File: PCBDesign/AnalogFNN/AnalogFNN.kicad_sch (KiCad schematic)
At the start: 7 parts, among them J1 Conn_01x04_Male, J2 Conn_01x05_Male, SW1 SW_SPDT, U1 STM32F030CCTx

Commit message: Finished neuron placement, laying out weight control modules
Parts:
- added J3: Conn_01x36_Male, Connector_PinHeader_1.00mm:PinHeader_1x36_P1.00mm_Vertical, symbol Connector:Conn_01x36_Male
- added J4: Conn_01x06_Male, Connector_PinHeader_1.00mm:PinHeader_1x06_P1.00mm_Vertical, symbol Connector:Conn_01x06_Male
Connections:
- new net L1_IN1: J3.1 (Pin_1)
- new net L1_IN10: J3.10 (Pin_10)
- new net L1_IN11: J3.11 (Pin_11)
- new net L1_IN12: J3.12 (Pin_12)
- new net L1_IN13: J3.13 (Pin_13)
- new net L1_IN14: J3.14 (Pin_14)
- new net L1_IN15: J3.15 (Pin_15)
- new net L1_IN16: J3.16 (Pin_16)
- new net L1_IN17: J3.17 (Pin_17)
- new net L1_IN18: J3.18 (Pin_18)
- new net L1_IN19: J3.19 (Pin_19)
- new net L1_IN2: J3.2 (Pin_2)
- new net L1_IN20: J3.20 (Pin_20)
- new net L1_IN21: J3.21 (Pin_21)
- new net L1_IN22: J3.22 (Pin_22)
- new net L1_IN23: J3.23 (Pin_23)
- new net L1_IN24: J3.24 (Pin_24)
- new net L1_IN25: J3.25 (Pin_25)
- new net L1_IN26: J3.26 (Pin_26)
- new net L1_IN27: J3.27 (Pin_27)
- new net L1_IN28: J3.28 (Pin_28)
- new net L1_IN29: J3.29 (Pin_29)
- new net L1_IN3: J3.3 (Pin_3)
- new net L1_IN30: J3.30 (Pin_30)
- new net L1_IN31: J3.31 (Pin_31)
- new net L1_IN32: J3.32 (Pin_32)
- new net L1_IN33: J3.33 (Pin_33)
- new net L1_IN34: J3.34 (Pin_34)
- new net L1_IN35: J3.35 (Pin_35)
- new net L1_IN36: J3.36 (Pin_36)
- new net L1_IN4: J3.4 (Pin_4)
- new net L1_IN5: J3.5 (Pin_5)
- new net L1_IN6: J3.6 (Pin_6)
- new net L1_IN7: J3.7 (Pin_7)
- new net L1_IN8: J3.8 (Pin_8)
- new net L1_IN9: J3.9 (Pin_9)
- new net L5_OUT1: J4.1 (Pin_1)
- new net L5_OUT2: J4.2 (Pin_2)
- new net L5_OUT3: J4.3 (Pin_3)
- new net L5_OUT4: J4.4 (Pin_4)
- new net L5_OUT5: J4.5 (Pin_5)
- new net L5_OUT6: J4.6 (Pin_6)

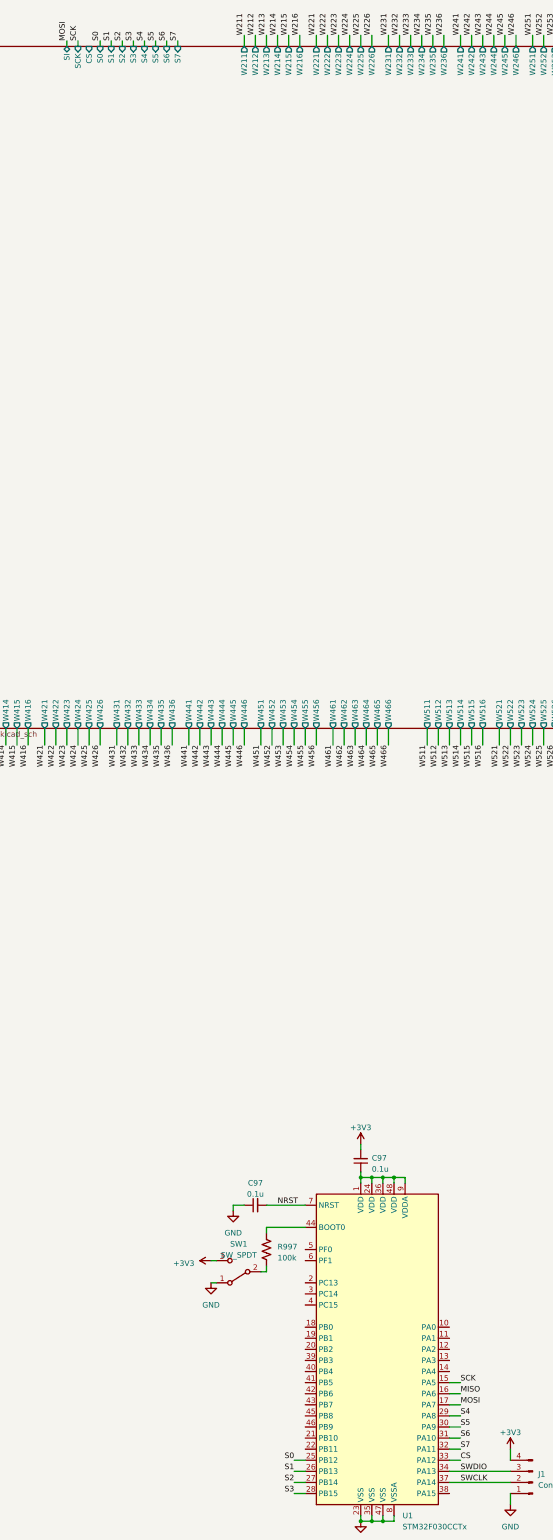
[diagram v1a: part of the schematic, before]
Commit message: Finished manual routing, working on autorouting
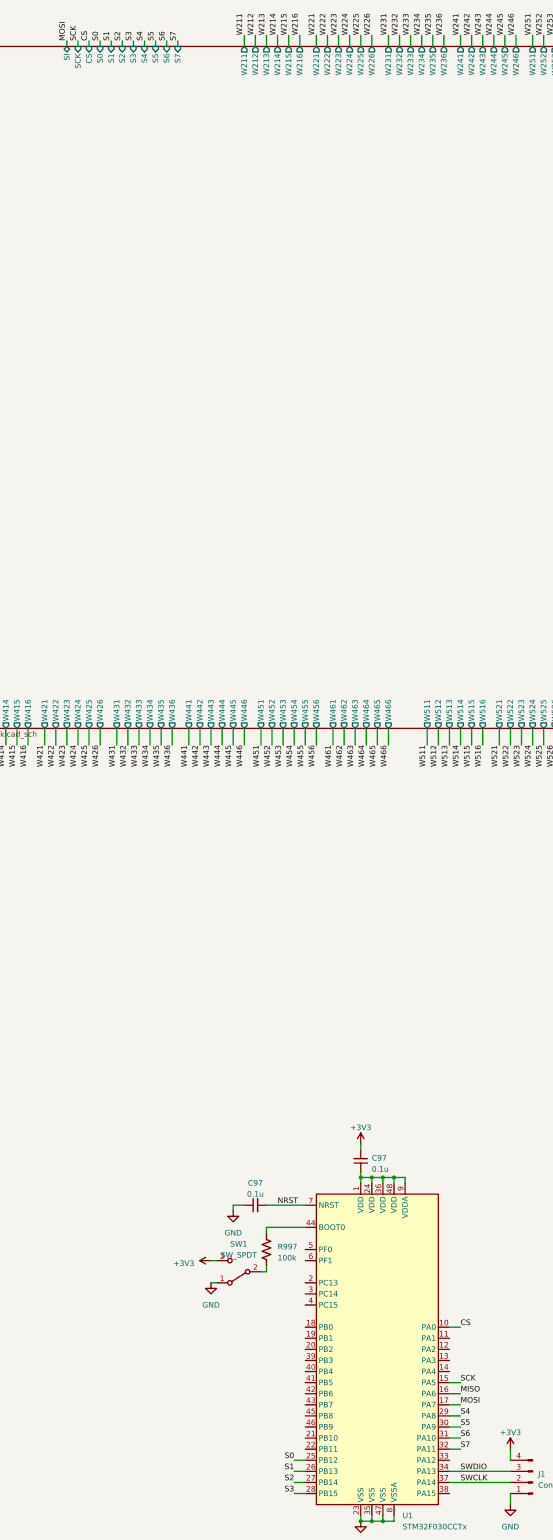
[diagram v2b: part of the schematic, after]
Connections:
- net CS: now also U1.10 (PA0); no longer U1.33 (PA12)
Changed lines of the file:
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@@
     (stroke (width 0) (type default))
   )
+  (wire (pts (xy 80.01 36.83) (xy 80.01 38.1))
+    (stroke (width 0) (type default))
+  )
   (wire (pts (xy 38.1 81.28) (xy 40.64 81.28))
     (stroke (width 0) (type default))
@@
     (stroke (width 0) (type default))
   )
-  (wire (pts (xy 162.56 361.95) (xy 165.1 361.95))
-    (stroke (width 0) (type default))
-  )
   (wire (pts (xy 346.71 313.69) (xy 349.25 313.69))
     (stroke (width 0) (type default))
@@
     (stroke (width 0) (type default))
   )
+  (wire (pts (xy 162.56 331.47) (xy 165.1 331.47))
+    (stroke (width 0) (type default))
+  )
   (wire (pts (xy 162.56 346.71) (xy 165.1 346.71))
     (stroke (width 0) (type default))
@@
     (effects (font (size 1.27 1.27)) (justify left bottom))
   )
+  (label "CS" (at 165.1 331.47 0) (fields_autoplaced)
+    (effects (font (size 1.27 1.27)) (justify left bottom))
+  )
   (label "L1_IN25" (at 346.71 346.71 180) (fields_autoplaced)
     (effects (font (size 1.27 1.27)) (justify right bottom))
@@
     (effects (font (size 1.27 1.27)) (justify left bottom))
   )
+  (label "CS" (at 80.01 36.83 90) (fields_autoplaced)
+    (effects (font (size 1.27 1.27)) (justify left bottom))
+  )
   (label "W551" (at 223.52 198.12 270) (fields_autoplaced)
     (effects (font (size 1.27 1.27)) (justify right bottom))
@@
     (effects (font (size 1.27 1.27)) (justify left bottom))
   )
-  (label "CS" (at 165.1 361.95 0) (fields_autoplaced)
-    (effects (font (size 1.27 1.27)) (justify left bottom))
-  )

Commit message: Footprint updates and redid NN in/out layers
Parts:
- removed J3: Conn_01x36_Male, Connector_PinHeader_1.00mm:PinHeader_1x36_P1.00mm_Vertical, symbol Connector:Conn_01x36_Male
- removed J4: Conn_01x06_Male, Connector_PinHeader_1.00mm:PinHeader_1x06_P1.00mm_Vertical, symbol Connector:Conn_01x06_Male
- added J3: Conn_01x12_Male, Connector_PinHeader_2.54mm:PinHeader_1x12_P2.54mm_Vertical, symbol Connector:Conn_01x12_Male
- added J4: Conn_01x02_Male, Connector_PinHeader_2.54mm:PinHeader_1x02_P2.54mm_Vertical, symbol Connector:Conn_01x02_Male
- J1: footprint Connector_PinHeader_1.00mm:PinHeader_1x04_P1.00mm_Vertical -> Connector_PinHeader_2.54mm:PinHeader_1x04_P2.54mm_Vertical
- J2: footprint Connector_PinHeader_1.00mm:PinHeader_1x05_P1.00mm_Vertical -> Connector_PinHeader_2.54mm:PinHeader_1x05_P2.54mm_Vertical
- SW1: footprint Connector_PinHeader_1.00mm:PinHeader_1x03_P1.00mm_Vertical -> Connector_PinHeader_2.54mm:PinHeader_1x03_P2.54mm_Vertical
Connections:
- net L1_IN1: now also J3.1 (Pin_1)
- net L1_IN10: now also J3.10 (Pin_10)
- net L1_IN11: now also J3.11 (Pin_11)
- net L1_IN12: now also J3.12 (Pin_12)
- net L1_IN2: now also J3.2 (Pin_2)
- net L1_IN3: now also J3.3 (Pin_3)
- net L1_IN4: now also J3.4 (Pin_4)
- net L1_IN5: now also J3.5 (Pin_5)
- net L1_IN6: now also J3.6 (Pin_6)
- net L1_IN7: now also J3.7 (Pin_7)
- net L1_IN8: now also J3.8 (Pin_8)
- net L1_IN9: now also J3.9 (Pin_9)
- net L5_OUT1: now also J4.1 (Pin_1)
- net L5_OUT2: now also J4.2 (Pin_2)
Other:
- removed sheet Neuron6_21
- removed sheet Neuron6_22
- removed sheet Neuron6_23
- removed sheet Neuron6_24
- removed sheet Neuron6_in1
- removed sheet Neuron6_in2
- removed sheet Neuron6_in3
- removed sheet Neuron6_in4
- removed sheet Neuron6_in5
- removed sheet Neuron6_in6
- added sheet InNeuron_1 (InNeuron.kicad_sch)
- added sheet InNeuron_2 (InNeuron.kicad_sch)
- added sheet InNeuron_3 (InNeuron.kicad_sch)
- added sheet InNeuron_4 (InNeuron.kicad_sch)
- added sheet InNeuron_5 (InNeuron.kicad_sch)
- added sheet InNeuron_6 (InNeuron.kicad_sch)
- sheet VariableWeights ports: added W1110, W1111, W1112, W117, W118, W119, W1210, W1211, W1212, W127, W128, W129, W1310, W1311, W1312, W137, W138, W139, W1410, W1411, W1412, W147, W148, W149, W1510, W1511, W1512, W157, W158, W159, W1610, W1611, W1612, W167, W168, W169; removed W531, W532, W533, W534, W535, W536, W541, W542, W543, W544, W545, W546, W551, W552, W553, W554, W555, W556, W561, W562, W563, W564, W565, W566

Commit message: Updated NN with non-activated outputs
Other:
- removed sheet Neuron6_19
- removed sheet Neuron6_20
- added sheet OutNeuron_1 (OutNeuron.kicad_sch)
- added sheet OutNeuron_2 (OutNeuron.kicad_sch)
